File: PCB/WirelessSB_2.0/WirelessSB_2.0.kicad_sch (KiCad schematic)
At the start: 23 parts, among them J1 Battery, SW1 PB1(Shift), SW10 PB7(R14), SW11 PB11, SW12 PB15, SW13 PB4(GTOut), SW14 PB8(Pos), SW15 PB12, SW16 PB16, SW2 PB5(HFoul), SW3 PB9(HScore), SW4 PB13(R24), SW5 PB2(Buzzer), SW6 PB6(GFoul), SW7 PB10(GScore), SW8 PB14(StartStop), SW9 PB3(HTOut), U1 ATmega328P-A, U2 AMS1117-3.3

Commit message: Done with the Controller main PCB
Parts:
- removed J1: Battery, Connector_PinHeader_1.27mm:PinHeader_1x02_P1.27mm_Vertical_SMD_Pin1Left, symbol Connector_Generic:Conn_01x02
- removed J?: NRF24L01, symbol Connector_Generic:Conn_01x08
- added C3, C4, C5: 100nF, Capacitor_SMD:C_1206_3216Metric_Pad1.33x1.80mm_HandSolder, symbol Device:C
- added D1: LED_ARGB, LED_THT:LED_D5.0mm-4_RGB, symbol Device:LED_ARGB
- added J1: Battery+Switch, Connector_Harwin:Harwin_M20-89003xx_1x03_P2.54mm_Horizontal, symbol Connector:Conn_01x03_Male
- added J2: OLED Display, Connector_Harwin:Harwin_M20-89004xx_1x04_P2.54mm_Horizontal, symbol Connector:Conn_01x04_Female
- added J3: FTDI Programmer, Connector_PinHeader_2.54mm:PinHeader_1x06_P2.54mm_Vertical, symbol Connector:Conn_01x06_Female
- added J4: Charging, symbol Connector:Conn_01x01_Female
- added R1: 330R, Resistor_SMD:R_1206_3216Metric_Pad1.30x1.75mm_HandSolder, symbol Device:R_US
- added R2: 100R, Resistor_SMD:R_1206_3216Metric_Pad1.30x1.75mm_HandSolder, symbol Device:R_US
- added R3, R4: 1K, Resistor_SMD:R_1206_3216Metric_Pad1.30x1.75mm_HandSolder, symbol Device:R_US
- added U3: NRF24L01_Breakout, mysensors_radios:NRF24L01-SMD, symbol RF:NRF24L01_Breakout
- C1, C2: renamed from C?; value C -> 22pF; footprint (none) -> Capacitor_SMD:C_1206_3216Metric_Pad1.33x1.80mm_HandSolder
- Y1: renamed from Y?; footprint (none) -> Crystal:Crystal_HC52-6mm_Vertical
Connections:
- net +3V3: now also U3.2 (VCC)
- net CSN: now also U1.14 (PB2), U3.4 (~{CSN})
- net GND: now also C4.1, C5.2, J1.3 (Pin_3), J2.4 (Pin_4), J3.5 (Pin_5), J3.6 (Pin_6), R2.2, R3.2, U3.1 (GND)
- net IRQ: now also U3.8 (IRQ)
- net MISO: now also U1.16 (PB4), U3.7 (MISO)
- net MOSI: now also U1.15 (PB3), U3.6 (MOSI)
- net NCE: now also U1.13 (PB1), U3.3 (CE)
- net SCK: now also U1.17 (PB5), U3.5 (SCK)
- net VCC: now also U1.18 (AVCC), U1.4 (VCC), U1.6 (VCC), C5.1, D1.1 (A), J1.1 (Pin_1), J2.3 (Pin_3), J3.4 (Pin_4), R1.1, R4.1
- net at U1.10 (PD6): now also J4.1 (Pin_1), R3.1
- net LED_RGB_R: now reaches U1.11 (PD7)
- net LED_RGB_R: now also D1.2 (RK)
- net LED_RGB_G: now reaches U1.12 (PB0)
- net LED_RGB_G: now also D1.3 (GK)
- net at U1.19 (ADC6): now also R1.2, R2.1
- net at U1.20 (AREF): now also C4.2
- net LED_RGB_B: now reaches U1.22 (ADC7)
- net LED_RGB_B: now also D1.4 (BK)
- net SDA: now reaches U1.27 (PC4)
- net SDA: now also J2.1 (Pin_1)
- net SCL: now reaches U1.28 (PC5)
- net SCL: now also J2.2 (Pin_2)
- net DTR: now reaches U1.29 (~{RESET}/PC6)
- net DTR: now also C3.1, R4.2
- net FTDI_TX: now reaches U1.30 (PD0)
- net FTDI_TX: now also J3.3 (Pin_3)
- net FTDI_RX: now reaches U1.31 (PD1)
- net FTDI_RX: now also J3.2 (Pin_2)
- new net: C3.2, J3.1 (Pin_1)
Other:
- note added: "10-09-2022"
- note added: "BATTERY INDICATOR"
- note added: "BUTTON MATRIX"
- note added: "Designed by: Kenny Neutron"
- note added: "POWER MANAGEMENT"
- note added: "PROGRAMMING INTERFACE"
- note added: "WIRELESS COMMUNICATION"
- note added: "Wireless BasketBall Scoreboard 2.0"
- moved on the sheet: C1, C2, SW1, SW10, SW11, SW12, SW13, SW14, SW15, SW16, SW2, SW3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

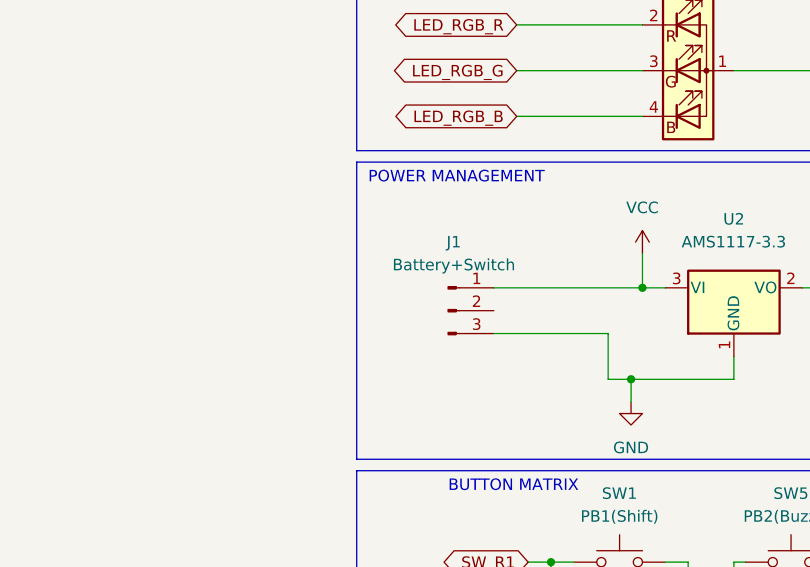
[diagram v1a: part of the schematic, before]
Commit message: FIXED: moved the BatteryIN & Capacitor to the bottom layer as it hits the charge controller
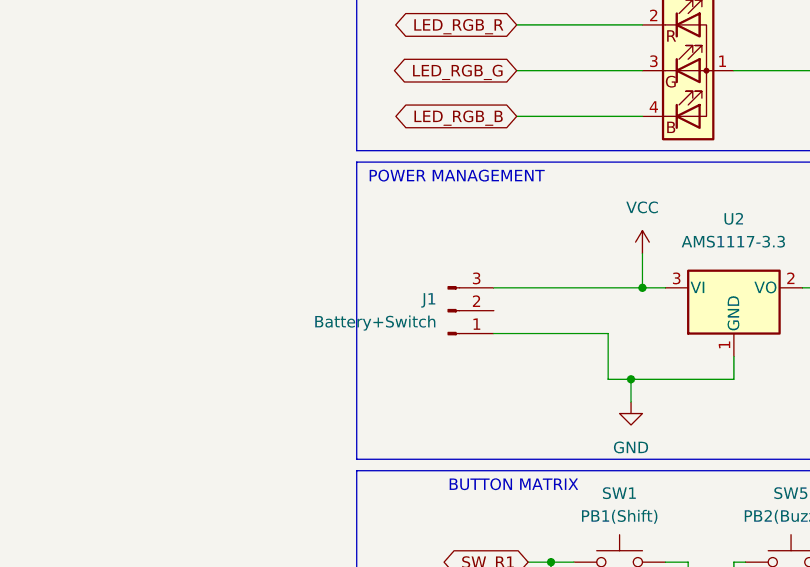
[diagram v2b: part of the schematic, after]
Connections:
- net GND: now also J1.1 (Pin_1); no longer J1.3 (Pin_3)
- net VCC: now also J1.3 (Pin_3); no longer J1.1 (Pin_1)

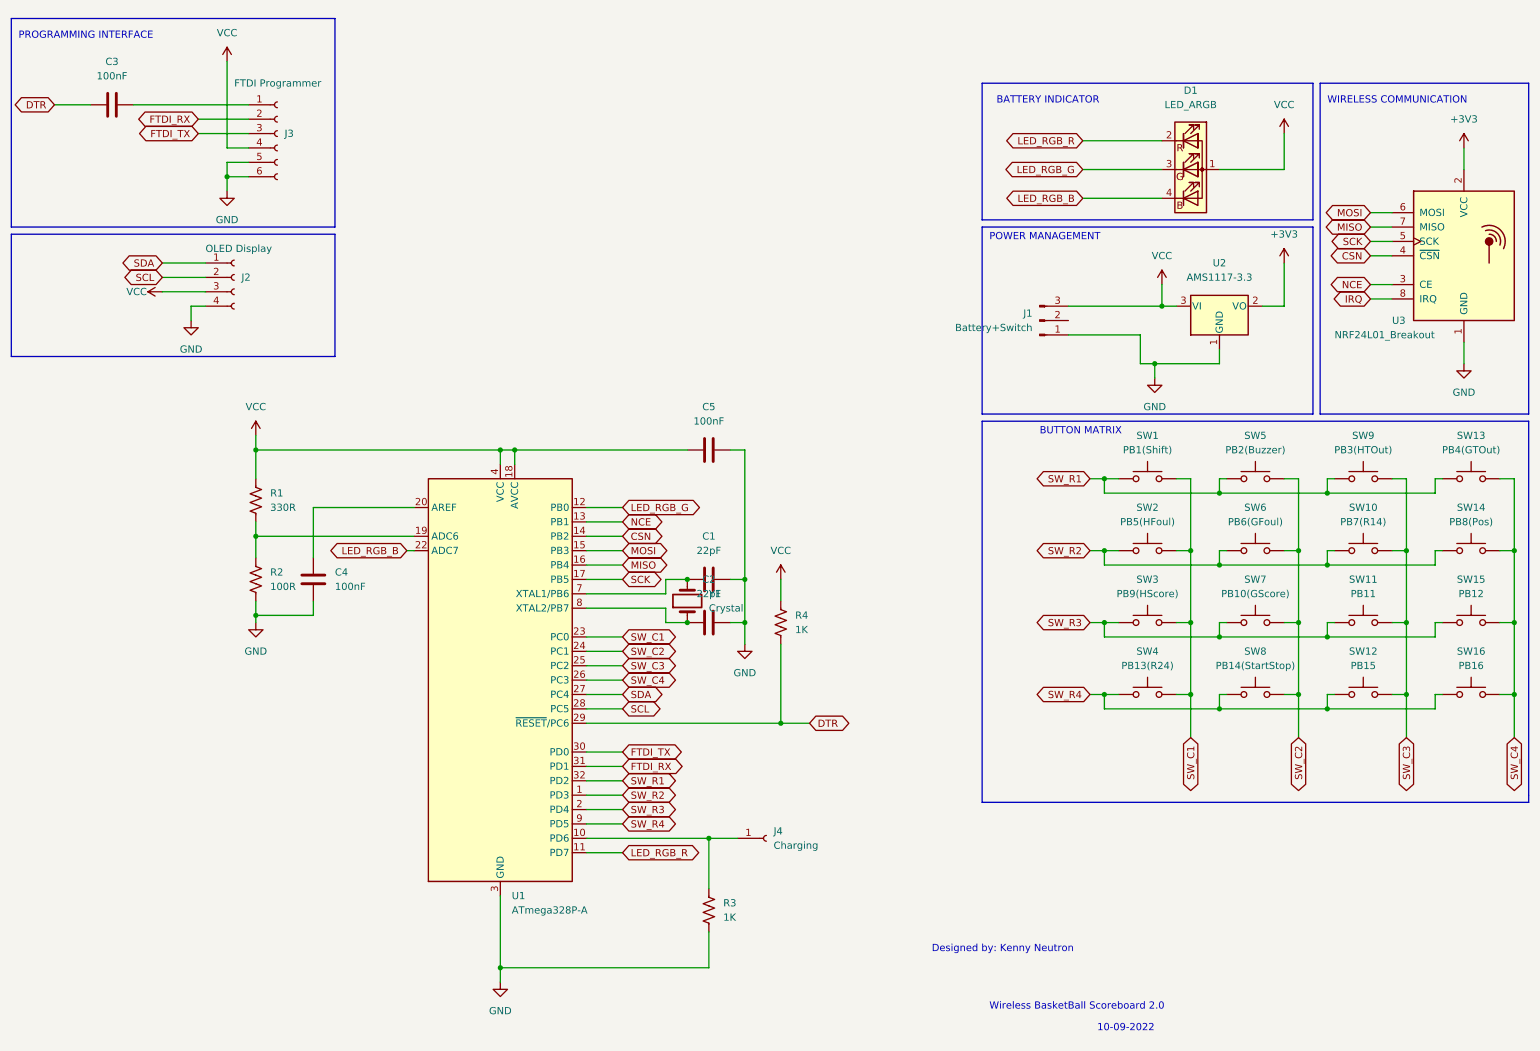
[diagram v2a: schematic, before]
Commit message: ADJUSTED: schematic diagram (ocd things :D) and ADDED: pdf file of the schematic from KiCAD
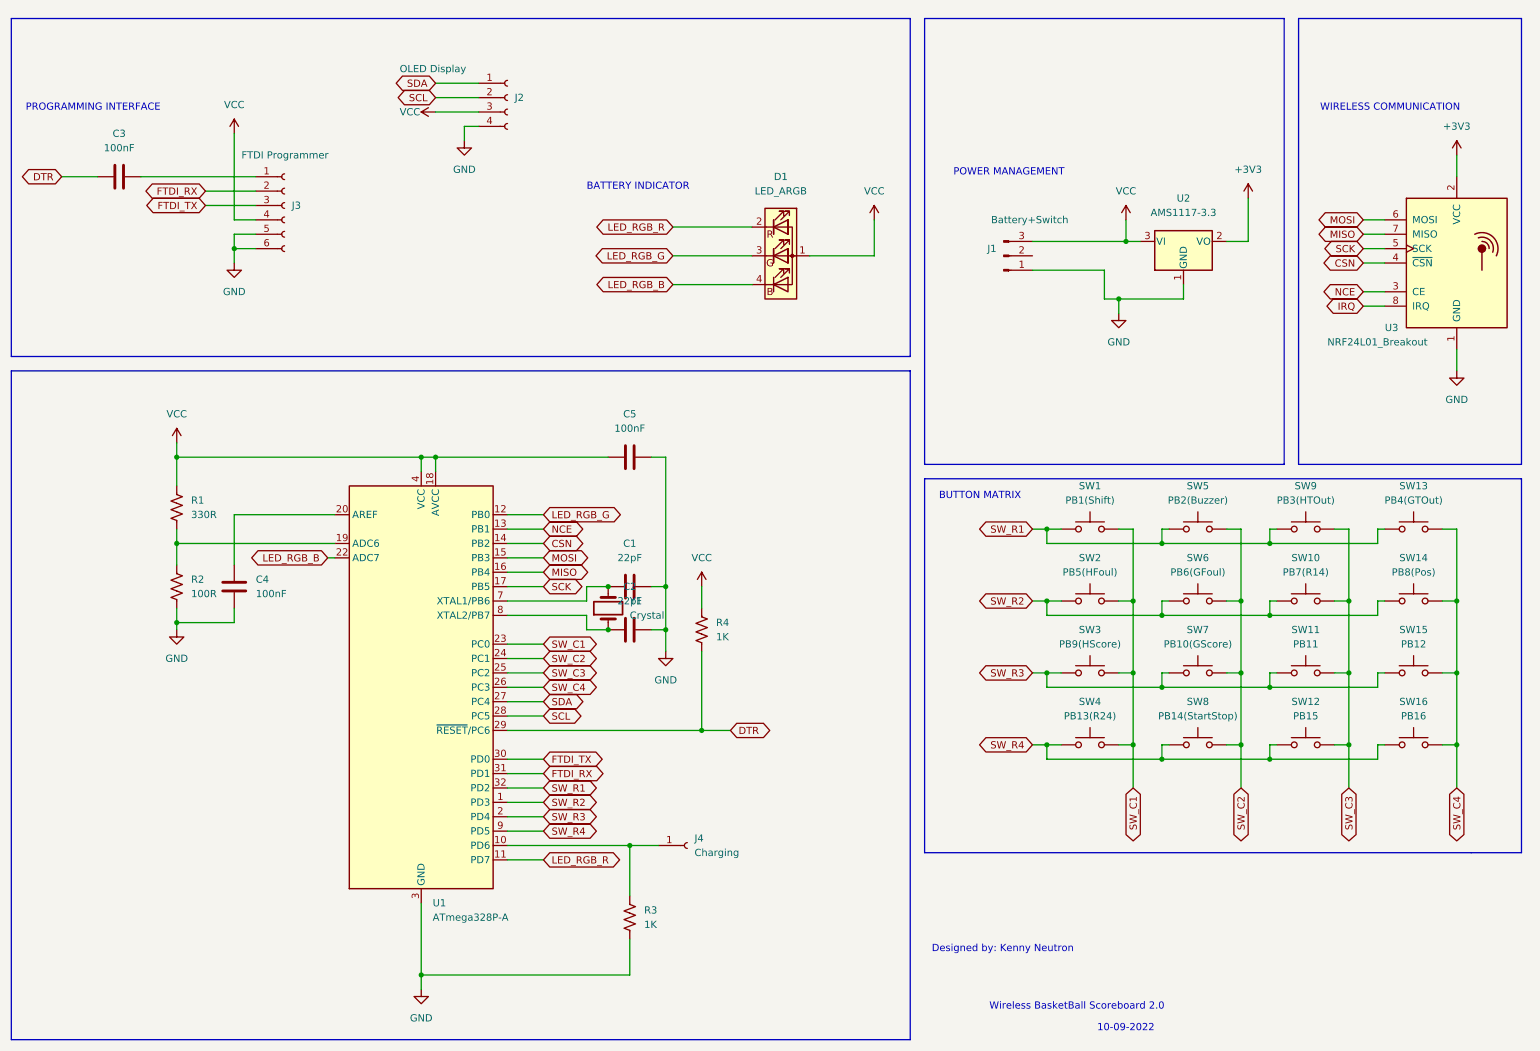
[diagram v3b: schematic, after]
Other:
- moved on the sheet: C1, C2, C3, C4, C5, D1, J1, J2, J3, J4, R1, R2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
